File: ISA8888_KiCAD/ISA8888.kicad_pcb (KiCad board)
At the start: 2 copper layers, 154.8 x 106.2 mm, 70 parts, among them J1 Bus_PCI_32bit_Universal, J2 Bus_ISA_16bit, J3 BALE/AEN/TC J3, J4 Crystal J4, J5 PCI Jumpers, J6 PPDGNT# Motherboard Redirect, J7 PPDREQ# Motherboard Redirect, U2 SMROM-AT24CS02, U4 LM7905_TO220, Y1 CFPS-72

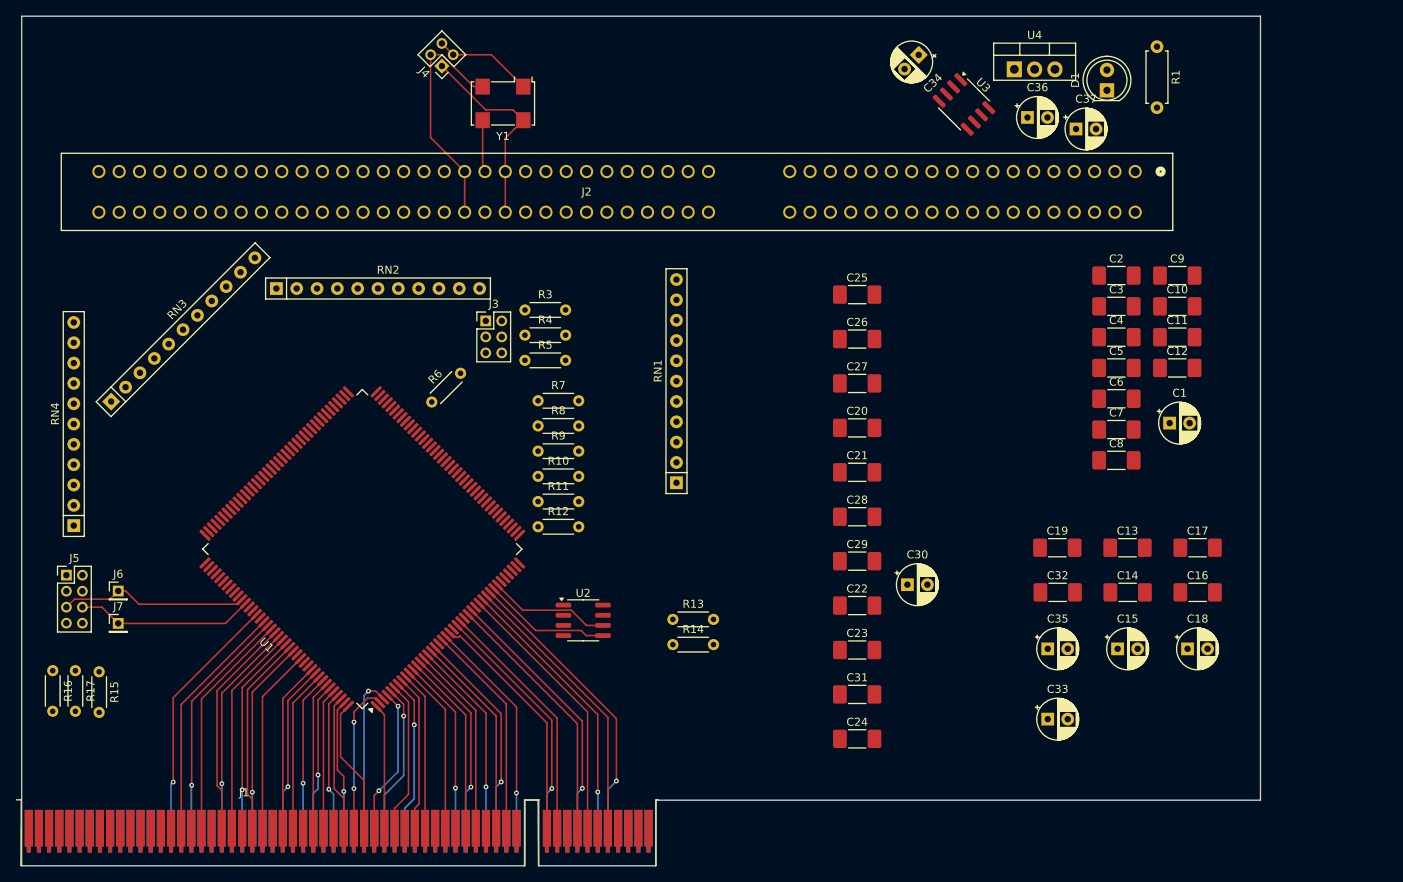
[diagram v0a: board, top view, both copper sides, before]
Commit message: Footprint fix and auto-routed
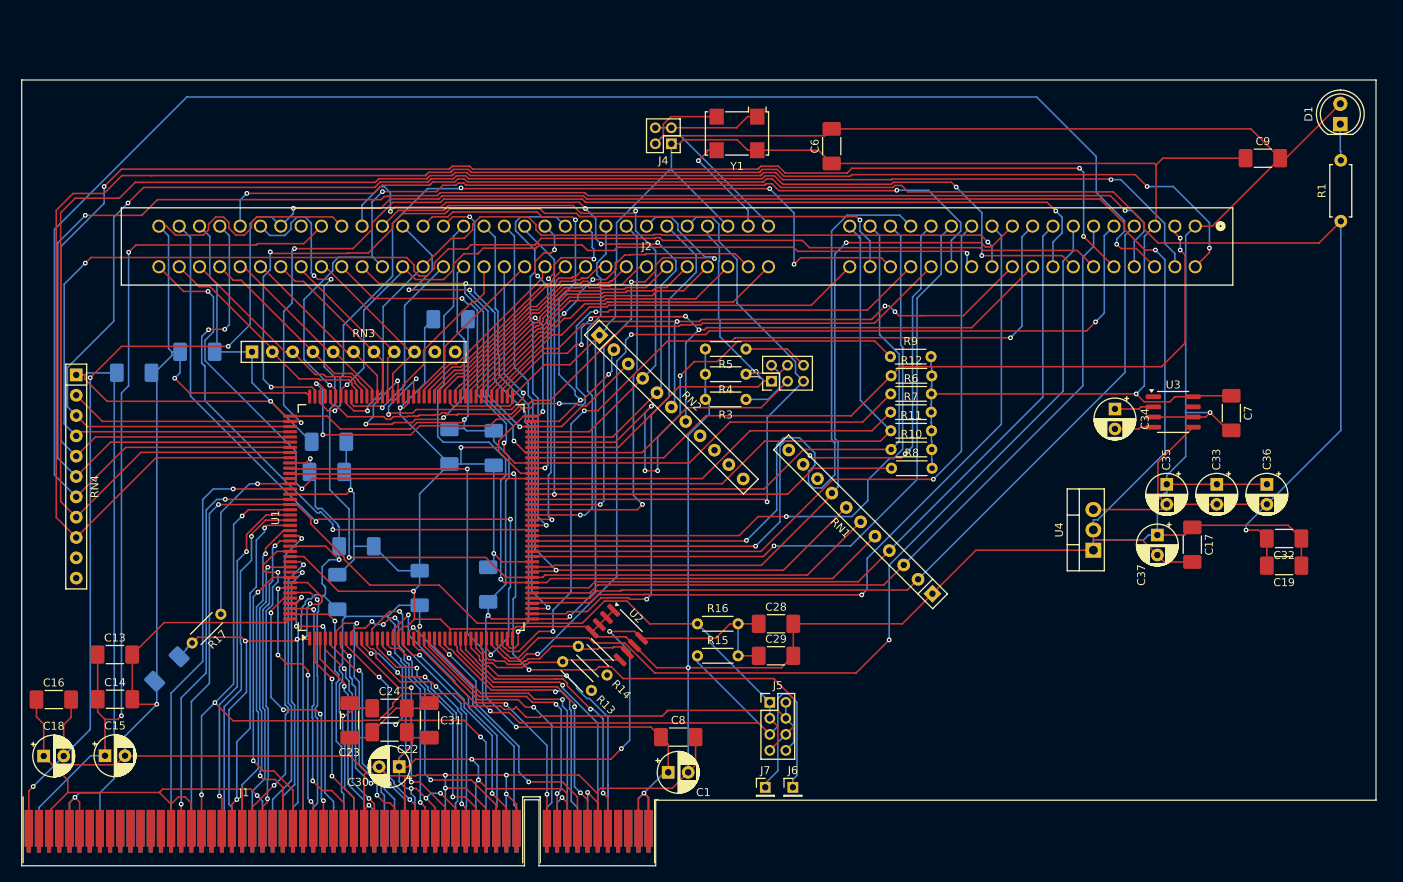
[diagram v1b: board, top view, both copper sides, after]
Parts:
- C10, C11, C12, C2, C20, C21, C25, C26, C27, C3, C4, C5: moved to B.Cu
- J2: footprint ISA8888:CONN_EBC49_SUL -> ISA8888:CONN_EBC49_SUL_Fixed
- J3: value BALE/AEN/TC J3 -> AEN/BALE/TC J3
- moved C16 143.6 mm to (84.2, 123.4)
- moved C18 143.6 mm to (82.9, 130.5)
- moved C11 130.5 mm to (94.2, 82.6)
- moved C14 127.3 mm to (91.8, 123.4)
- moved C13 127.3 mm to (91.8, 117.8)
- moved C15 127.3 mm to (90.6, 130.4)
- moved C12 122.5 mm to (102.1, 80.0), turned to 180 degrees
- moved C5 98.9 mm to (118.6, 91.2)
- moved C20 91.4 mm to (98.3, 119.6), turned to -135 degrees
- moved C10 90.8 mm to (133.8, 75.9), turned to 180 degrees
- moved J5 89.4 mm to (173.7, 123.8)
- moved J6 87.8 mm to (176.6, 134.4)
- moved C3 85.9 mm to (138.5, 109.0), turned to 90 degrees
- moved C4 84.5 mm to (133.6, 91.8), turned to -90 degrees
- moved J7 83.4 mm to (173.1, 134.4)
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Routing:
- net GND: track 46.5 -> 1002.6 mm, vias 0 -> 18
- net +5V: track 25.4 -> 562.1 mm, vias 0 -> 8
- net +3.3V: track 15.7 -> 344.0 mm, vias 0 -> 14
- net -12V: track 0.00 -> 278.4 mm, vias 0 -> 5
- net -5V: track 0.00 -> 231.4 mm, vias 0 -> 2
- net SD15: track 0.00 -> 229.2 mm, vias 0 -> 2
- net SD13: track 0.00 -> 222.7 mm, vias 0 -> 1
- net SD14: track 0.00 -> 218.6 mm, vias 0 -> 1
- net SD12: track 0.00 -> 204.6 mm, vias 0 -> 2
- net SD11: track 0.00 -> 202.8 mm, vias 0 -> 3
- net SD9: track 0.00 -> 185.4 mm, vias 0 -> 3
- net SD10: track 0.00 -> 182.3 mm, vias 0 -> 1
- net SD8: track 0.00 -> 159.3 mm, vias 0 -> 3
- net DACK7#: track 0.00 -> 124.3 mm, vias 0 -> 3
- net DRQ2: track 0.00 -> 122.4 mm, vias 0 -> 3
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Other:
- board size 154.8 x 106.2 mm -> 169.3 x 98.2 mm

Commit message: ISA8888 PCB update
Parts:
- moved C32 5.37 mm to (236.7, 108.5), turned to 0 degrees
- moved R1 2.70 mm to (245.1, 66.3)
- moved C19 1.99 mm to (236.7, 105.1), turned to 0 degrees
- moved U4 0.66 mm to (214.1, 104.1)
- moved C6 0.36 mm to (181.4, 53.9)
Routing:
- net GND: track 1002.6 -> 972.2 mm, vias 18 -> 23
- net IRQ3: track 61.7 -> 47.7 mm
- net -5V: track 231.4 -> 240.5 mm, vias 2 -> 3
- net AD0: track 46.9 -> 39.0 mm
- net IOW#: track 57.0 -> 52.0 mm
- net +5V: track 562.1 -> 557.8 mm
- net -12V: track 278.4 -> 274.8 mm
- net DEVSEL#: track 34.8 -> 31.5 mm
- net C/BE3#: track 40.7 -> 37.6 mm
- net PERR#: track 38.1 -> 35.0 mm
- net AD1: track 39.0 -> 35.9 mm
- net AD3: track 38.2 -> 35.1 mm
- net IREQ#: track 133.6 -> 130.7 mm
- net AD27: track 43.4 -> 40.4 mm
- net AD25: track 42.4 -> 39.6 mm
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
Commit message: ISA8888 Prototype Rev 00
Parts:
- added G***: LOGO, DFT:DFT_SS_Small, F.Cu at (204.2, 109.5)
- added G***: LOGO, DFT:DFT_Logo_Small, F.Cu at (210.5, 128.1)
- added G***: LOGO, DFT:DFT_SS_Medium, B.Cu at (127.8, 92.2)
- added G***: LOGO, DFT:DFT_Logo_Medium, B.Cu at (207.1, 92.3)
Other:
- outline, holes or cut-outs redrawn
- board text added: "ISA8888 Prototype DartFrogTek"
